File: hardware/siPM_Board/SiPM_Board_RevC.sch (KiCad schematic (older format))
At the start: 24 parts, among them J1 Conn_02x34_Odd_Even, J2 Conn_02x34_Odd_Even, U1 LM94021, U2 S14161-6050HS-04, U3 S14161-6050HS-04, U4 S14161-6050HS-04, U5 S14161-6050HS-04

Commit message: SiPM Board RevC modified
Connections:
- net BIAS3: now also J2.1 (Pin_1); no longer J2.68 (Pin_68)
- net BIAS4: now also J2.67 (Pin_67); no longer J2.2 (Pin_2)
- net GND: now also J2.11 (Pin_11), J2.13 (Pin_13), J2.15 (Pin_15), J2.17 (Pin_17), J2.19 (Pin_19), J2.21 (Pin_21), J2.23 (Pin_23), J2.25 (Pin_25), J2.27 (Pin_27), J2.29 (Pin_29), J2.3 (Pin_3), J2.31 (Pin_31), J2.33 (Pin_33), J2.35 (Pin_35), J2.37 (Pin_37), J2.39 (Pin_39), J2.41 (Pin_41), J2.43 (Pin_43), J2.45 (Pin_45), J2.47 (Pin_47), J2.49 (Pin_49), J2.5 (Pin_5), J2.51 (Pin_51), J2.53 (Pin_53), J2.55 (Pin_55), J2.57 (Pin_57), J2.59 (Pin_59), J2.61 (Pin_61), J2.63 (Pin_63), J2.65 (Pin_65), J2.7 (Pin_7), J2.9 (Pin_9); no longer J2.10 (Pin_10), J2.12 (Pin_12), J2.14 (Pin_14), J2.16 (Pin_16), J2.18 (Pin_18), J2.20 (Pin_20), J2.22 (Pin_22), J2.24 (Pin_24), J2.26 (Pin_26), J2.28 (Pin_28), J2.30 (Pin_30), J2.32 (Pin_32), J2.34 (Pin_34), J2.36 (Pin_36), J2.38 (Pin_38), J2.4 (Pin_4), J2.40 (Pin_40), J2.42 (Pin_42), J2.44 (Pin_44), J2.46 (Pin_46), J2.48 (Pin_48), J2.50 (Pin_50), J2.52 (Pin_52), J2.54 (Pin_54), J2.56 (Pin_56), J2.58 (Pin_58), J2.6 (Pin_6), J2.60 (Pin_60), J2.62 (Pin_62), J2.64 (Pin_64), J2.66 (Pin_66), J2.8 (Pin_8)
- net at U5.A2 (A1A): now also J2.34 (Pin_34); no longer J2.35 (Pin_35)
- net at U5.A4 (A2A): now also J2.42 (Pin_42); no longer J2.27 (Pin_27)
- net at U5.A6 (A3A): now also J2.50 (Pin_50); no longer J2.19 (Pin_19)
- net at U5.A8 (A4A): now also J2.58 (Pin_58); no longer J2.11 (Pin_11)
- net at U5.C2 (B1A): now also J2.36 (Pin_36); no longer J2.33 (Pin_33)
- net at U5.C4 (B2A): now also J2.44 (Pin_44); no longer J2.25 (Pin_25)
- net at U5.C6 (B3A): now also J2.52 (Pin_52); no longer J2.17 (Pin_17)
- net at U5.C8 (B4A): now also J2.60 (Pin_60); no longer J2.9 (Pin_9)
- net at U5.E1 (C1A): now also J2.38 (Pin_38); no longer J2.31 (Pin_31)
- net at U5.E3 (C2A): now also J2.46 (Pin_46); no longer J2.23 (Pin_23)
- net at U5.E5 (C3A): now also J2.54 (Pin_54); no longer J2.15 (Pin_15)
- net at U5.E7 (C4A): now also J2.62 (Pin_62); no longer J2.7 (Pin_7)
- net at U5.G1 (D1A): now also J2.40 (Pin_40); no longer J2.29 (Pin_29)
- net at U5.G3 (D2A): now also J2.48 (Pin_48); no longer J2.21 (Pin_21)
- net at U5.G5 (D3A): now also J2.56 (Pin_56); no longer J2.13 (Pin_13)
- net at U5.G7 (D4A): now also J2.64 (Pin_64); no longer J2.5 (Pin_5)
- net at U4.A2 (A1A): now also J2.2 (Pin_2); no longer J2.67 (Pin_67)
- net at U4.A4 (A2A): now also J2.10 (Pin_10); no longer J2.59 (Pin_59)
- net at U4.A6 (A3A): now also J2.18 (Pin_18); no longer J2.51 (Pin_51)
- net at U4.A8 (A4A): now also J2.26 (Pin_26); no longer J2.43 (Pin_43)
- net at U4.C2 (B1A): now also J2.4 (Pin_4); no longer J2.65 (Pin_65)
- net at U4.C4 (B2A): now also J2.12 (Pin_12); no longer J2.57 (Pin_57)
- net at U4.C6 (B3A): now also J2.20 (Pin_20); no longer J2.49 (Pin_49)
- net at U4.C8 (B4A): now also J2.28 (Pin_28); no longer J2.41 (Pin_41)
- net at U4.E1 (C1A): now also J2.6 (Pin_6); no longer J2.63 (Pin_63)
- net at U4.E3 (C2A): now also J2.14 (Pin_14); no longer J2.55 (Pin_55)
- net at U4.E5 (C3A): now also J2.22 (Pin_22); no longer J2.47 (Pin_47)
- net at U4.E7 (C4A): now also J2.30 (Pin_30); no longer J2.39 (Pin_39)
- net at U4.G1 (D1A): now also J2.8 (Pin_8); no longer J2.61 (Pin_61)
- net at U4.G3 (D2A): now also J2.16 (Pin_16); no longer J2.53 (Pin_53)
- net at U4.G5 (D3A): now also J2.24 (Pin_24); no longer J2.45 (Pin_45)
- net at U4.G7 (D4A): now also J2.32 (Pin_32); no longer J2.37 (Pin_37)
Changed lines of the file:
@@
 L SiPM_Board-rescue:Conn_02x34_Odd_Even-Connector_Generic J2
 U 1 1 61207A16
-P 9350 3550
-F 0 "J2" H 8975 1525 50  0000 R CNN
-F 1 "Conn_02x34_Odd_Even" H 9750 1650 50  0000 R CNN
-F 2 "Arich_SiPM_Footprints:MW-34-03-G-D-245-065-ES" H 9350 3550 50  0001 C CNN
-F 3 "http://suddendocs.samtec.com/prints/mw-xx-03-x-d-xxx-xxx-xx-footprint.pdf" H 9350 3550 50  0001 C CNN
-F 4 "MW-34-03-G-D-245-065-ES" H 9350 3550 50  0001 C CNN "MFN"
-F 5 "Samtec" H 9350 3550 50  0001 C CNN "Supplier"
-F 6 "MW-34-03-G-D-245-065-ES" H 9350 3550 50  0001 C CNN "Supplier P/N"
-F 7 "$0" H 9350 3550 50  0001 C CNN "Item Cost"
-	1    9350 3550
-	1    0    0    1
+P 9450 3450
+F 0 "J2" H 9075 1425 50  0000 R CNN
+F 1 "Conn_02x34_Odd_Even" H 9850 1550 50  0000 R CNN
+F 2 "Arich_SiPM_Footprints:MW-34-03-G-D-245-065-ES" H 9450 3450 50  0001 C CNN
+F 3 "http://suddendocs.samtec.com/prints/mw-xx-03-x-d-xxx-xxx-xx-footprint.pdf" H 9450 3450 50  0001 C CNN
+F 4 "MW-34-03-G-D-245-065-ES" H 9450 3450 50  0001 C CNN "MFN"
+F 5 "Samtec" H 9450 3450 50  0001 C CNN "Supplier"
+F 6 "MW-34-03-G-D-245-065-ES" H 9450 3450 50  0001 C CNN "Supplier P/N"
+F 7 "$0" H 9450 3450 50  0001 C CNN "Item Cost"
+	1    9450 3450
+	-1   0    0    -1
 $EndComp
 Wire Wire Line

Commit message: Fixing SiPM Libraries
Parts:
- C1, C10, C11, C12, C13, C14, C15, C16, C17, C2, C3, C4, C5, C6, C7, C8, C9: symbol SiPM_Board-rescue:C-Device -> Device:C
- J1, J2: symbol SiPM_Board-rescue:Conn_02x34_Odd_Even-Connector_Generic -> Connector_Generic:Conn_02x34_Odd_Even
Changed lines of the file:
@@
 	3750 4250 3750 3850
 $Comp
-L SiPM_Board-rescue:Conn_02x34_Odd_Even-Connector_Generic J1
+L Connector_Generic:Conn_02x34_Odd_Even J1
 U 1 1 601F94DF
 P 5000 3450
@@
 Connection ~ 5500 2050
 $Comp
-L SiPM_Board-rescue:GND-power #PWR04
+L power:GND #PWR04
 U 1 1 603E3F9A
 P 5500 5250
@@
 	8100 4250 8100 3850
 $Comp
-L SiPM_Board-rescue:Conn_02x34_Odd_Even-Connector_Generic J2
+L Connector_Generic:Conn_02x34_Odd_Even J2
 U 1 1 61207A16
 P 9450 3450
@@
 Connection ~ 9850 2050
 $Comp
-L SiPM_Board-rescue:GND-power #PWR07
+L power:GND #PWR07
 U 1 1 61207A7A
 P 9850 5250
@@
 OUT
 $Comp
-L SiPM_Board-rescue:C-Device C16
+L Device:C C16
 U 1 1 604DBA71
 P 6700 1100
@@
 $EndComp
 $Comp
-L SiPM_Board-rescue:C-Device C14
+L Device:C C14
 U 1 1 604DBA63
 P 6400 1100
@@
 	6400 1300 6400 1250
 $Comp
-L SiPM_Board-rescue:GND-power #PWR05
+L power:GND #PWR05
 U 1 1 6023C2FA
 P 6250 1400
@@
 BIAS2
 $Comp
-L SiPM_Board-rescue:C-Device C8
+L Device:C C8
 U 1 1 60DAF07F
 P 2350 3800
@@
 $EndComp
 $Comp
-L SiPM_Board-rescue:C-Device C6
+L Device:C C6
 U 1 1 60DAF08D
 P 2050 3800
@@
 	2050 4000 2050 3950
 $Comp
-L SiPM_Board-rescue:GND-power #PWR02
+L power:GND #PWR02
 U 1 1 60DAF09E
 P 1900 4100
@@
 	2050 1300 2050 1250
 $Comp
-L SiPM_Board-rescue:GND-power #PWR01
+L power:GND #PWR01
 U 1 1 60F1D723
 P 1900 1400
@@
 BIAS4
 $Comp
-L SiPM_Board-rescue:C-Device C17
+L Device:C C17
 U 1 1 60F797D1
 P 6700 3850
@@
 $EndComp
 $Comp
-L SiPM_Board-rescue:C-Device C15
+L Device:C C15
 U 1 1 60F797DF
 P 6400 3850
@@
 Connection ~ 2650 6700
 $Comp
-L SiPM_Board-rescue:C-Device C9
+L Device:C C9
 U 1 1 6056E72C
 P 2650 6850
@@
 	2750 7100 2700 7100
 $Comp
-L SiPM_Board-rescue:GND-power #PWR03
+L power:GND #PWR03
 U 1 1 612A80CE
 P 3100 7500
@@
 BIAS3
 $Comp
-L SiPM_Board-rescue:GND-power #PWR06
+L power:GND #PWR06
 U 1 1 602B2E79
 P 6250 4150
@@
 	4800 5150 4750 5150
 $Comp
-L SiPM_Board-rescue:C-Device C3
+L Device:C C3
 U 1 1 60372068
 P 1750 1100
@@
 $EndComp
 $Comp
-L SiPM_Board-rescue:C-Device C1
+L Device:C C1
 U 1 1 6037BC42
 P 1450 1100
@@
 $EndComp
 $Comp
-L SiPM_Board-rescue:C-Device C4
+L Device:C C4
 U 1 1 6037EBF4
 P 1750 3800
@@
 $EndComp
 $Comp
-L SiPM_Board-rescue:C-Device C2
+L Device:C C2
 U 1 1 6037EC10
 P 1450 3800
@@
 $EndComp
 $Comp
-L SiPM_Board-rescue:C-Device C13
+L Device:C C13
 U 1 1 603C9FC8
 P 6100 3850
@@
 $EndComp
 $Comp
-L SiPM_Board-rescue:C-Device C11
+L Device:C C11
 U 1 1 603C9FE4
 P 5800 3850
@@
 $EndComp
 $Comp
-L SiPM_Board-rescue:C-Device C12
+L Device:C C12
 U 1 1 60413ED0
 P 6100 1100
@@
 $EndComp
 $Comp
-L SiPM_Board-rescue:C-Device C10
+L Device:C C10
 U 1 1 60413EDE
 P 5800 1100
@@
 $EndComp
 $Comp
-L SiPM_Board-rescue:C-Device C5
+L Device:C C5
 U 1 1 60F1D712
 P 2050 1100
@@
 $EndComp
 $Comp
-L SiPM_Board-rescue:C-Device C7
+L Device:C C7
 U 1 1 60F1D704
 P 2350 1100

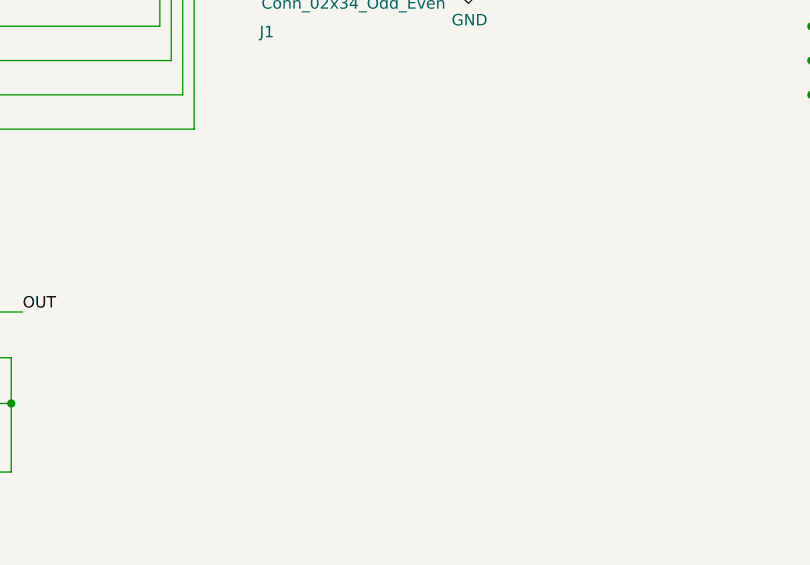
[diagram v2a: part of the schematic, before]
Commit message: Branch to add PEM nuts to SiPM board
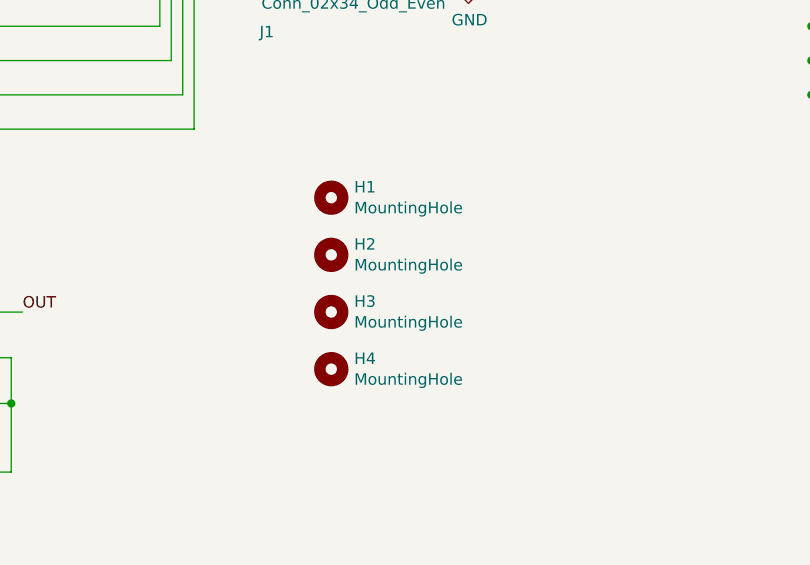
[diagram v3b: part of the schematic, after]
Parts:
- added H1, H2, H3, H4: MountingHole, Arich_SiPM_Footprints:SMTSO-nut-0-80, symbol Mechanical:MountingHole
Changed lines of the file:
@@
 NoConn ~ 9150 5050
 NoConn ~ 9150 5150
+$Comp
+L Mechanical:MountingHole H1
+U 1 1 60E1713D
+P 4900 6200
+F 0 "H1" H 5000 6246 50  0000 L CNN
+F 1 "MountingHole" H 5000 6155 50  0000 L CNN
+F 2 "Arich_SiPM_Footprints:SMTSO-nut-0-80" H 4900 6200 50  0001 C CNN
+F 3 "~" H 4900 6200 50  0001 C CNN
+	1    4900 6200
+	1    0    0    -1
+$EndComp
+$Comp
+L Mechanical:MountingHole H2
+U 1 1 60E1A6B8
+P 4900 6450
+F 0 "H2" H 5000 6496 50  0000 L CNN
+F 1 "MountingHole" H 5000 6405 50  0000 L CNN
+F 2 "Arich_SiPM_Footprints:SMTSO-nut-0-80" H 4900 6450 50  0001 C CNN
+F 3 "~" H 4900 6450 50  0001 C CNN
+	1    4900 6450
+	1    0    0    -1
+$EndComp
+$Comp
+L Mechanical:MountingHole H3
+U 1 1 60E1AF09
+P 4900 6700
+F 0 "H3" H 5000 6746 50  0000 L CNN
+F 1 "MountingHole" H 5000 6655 50  0000 L CNN
+F 2 "Arich_SiPM_Footprints:SMTSO-nut-0-80" H 4900 6700 50  0001 C CNN
+F 3 "~" H 4900 6700 50  0001 C CNN
+	1    4900 6700
+	1    0    0    -1
+$EndComp
+$Comp
+L Mechanical:MountingHole H4
+U 1 1 60E1B743
+P 4900 6950
+F 0 "H4" H 5000 6996 50  0000 L CNN
+F 1 "MountingHole" H 5000 6905 50  0000 L CNN
+F 2 "Arich_SiPM_Footprints:SMTSO-nut-0-80" H 4900 6950 50  0001 C CNN
+F 3 "~" H 4900 6950 50  0001 C CNN
+	1    4900 6950
+	1    0    0    -1
+$EndComp
 $EndSCHEMATC
